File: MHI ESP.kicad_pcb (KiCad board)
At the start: 2 copper layers, 26 x 35 mm, 9 parts, among them J1 , U1 WeMos_D1_mini, U2 R-78E5.0-1.0, U3 DS18B20U, U4 TXB0104PW

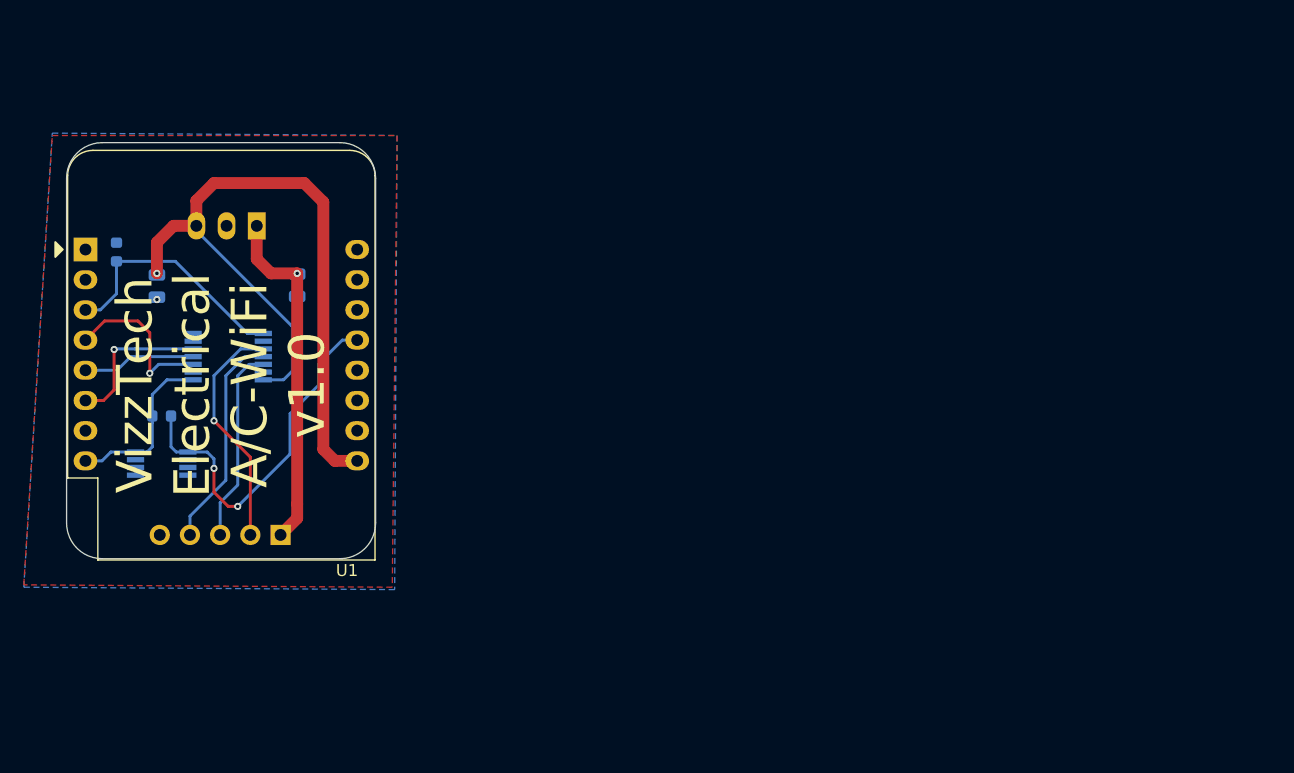
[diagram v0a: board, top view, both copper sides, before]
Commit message: Re-annotate schematic and update components on PCB, ready for new track layout
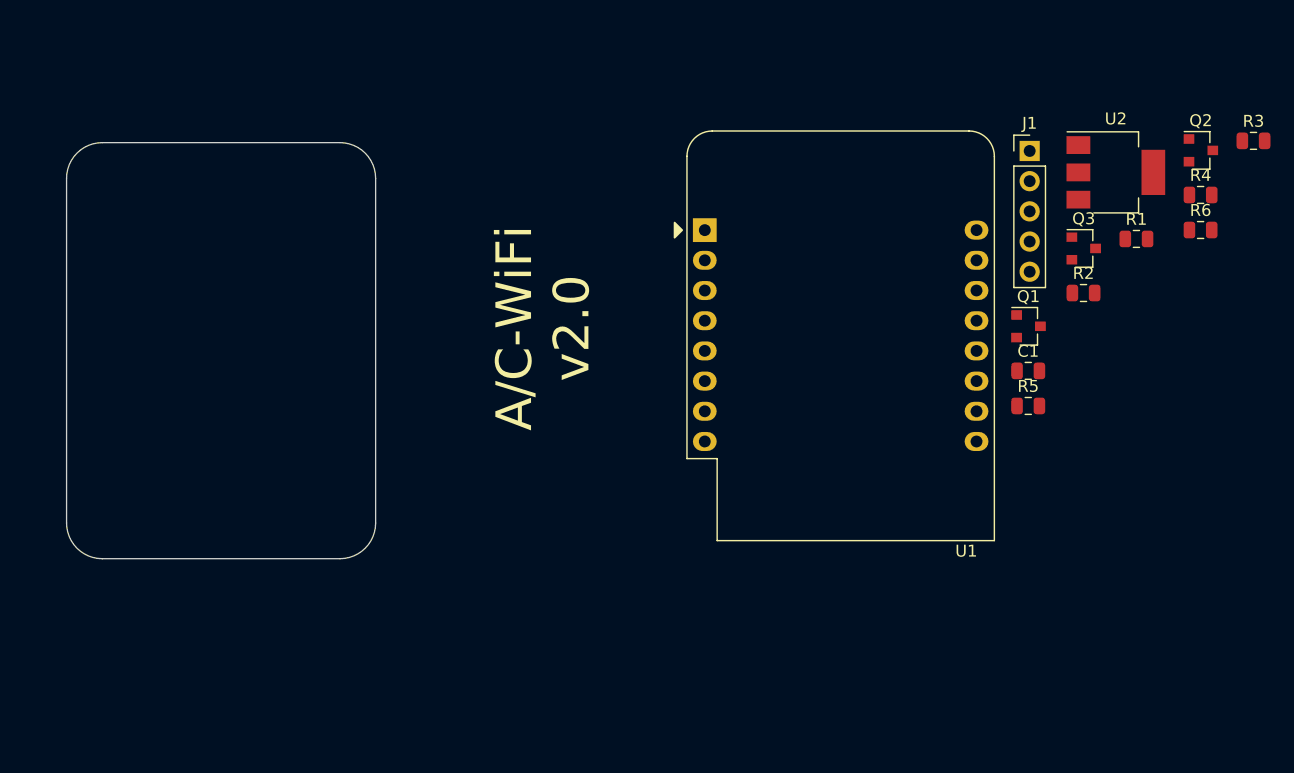
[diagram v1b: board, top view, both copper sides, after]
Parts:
- removed C2: 10uF, 0805, Capacitor_SMD:C_0805_2012Metric
- removed U3: DS18B20U, Package_SO:MSOP-8_3x3mm_P0.65mm
- removed U4: TXB0104PW, Package_SO:TSSOP-14_4.4x5mm_P0.65mm
- added Q1: BSS138, Package_TO_SOT_SMD:SOT-23, F.Cu at (192.9, 99.5)
- added Q2: BSS138, Package_TO_SOT_SMD:SOT-23, F.Cu at (207.4, 84.7)
- added Q3: BSS138, Package_TO_SOT_SMD:SOT-23, F.Cu at (197.6, 92.9)
- added R3: 10k, Resistor_SMD:R_0805_2012Metric, F.Cu at (211.8, 83.8)
- added R4: 10k, Resistor_SMD:R_0805_2012Metric, F.Cu at (207.4, 88.4)
- added R5: 10k, Resistor_SMD:R_0805_2012Metric, F.Cu at (192.9, 106.2)
- added R6: 10k, Resistor_SMD:R_0805_2012Metric, F.Cu at (207.4, 91.3)
- C1, J1: moved to F.Cu
- R1: value 100k, 0603 -> 10k; footprint Resistor_SMD:R_0603_1608Metric -> Resistor_SMD:R_0805_2012Metric; moved to F.Cu
- R2: value 4k7, 0603 -> 10k; footprint Resistor_SMD:R_0603_1608Metric -> Resistor_SMD:R_0805_2012Metric; moved to F.Cu
- U2: value R-78E5.0-1.0 -> LD1117S50TR; footprint Converter_DCDC:Converter_DCDC_RECOM_R-78E-0.5_THT -> Package_TO_SOT_SMD:SOT-223-3_TabPin2; moved to F.Cu
- moved R1 85.8 mm to (202.0, 92.1), turned to 0 degrees
- moved R2 78.2 mm to (197.6, 96.7)
- moved U2 72.4 mm to (200.3, 86.5), turned to 0 degrees
- moved J1 70.8 mm to (193.0, 84.7), turned to 0 degrees
- moved C1 61.9 mm to (192.9, 103.2), turned to 0 degrees
- moved U1 52.1 mm to (165.7, 91.4)
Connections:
- C1 pad 1: +12V -> +5V
- J1 pad 2: Net-(J1-Pad2) -> MHI-MOSI
- J1 pad 3: Net-(J1-Pad3) -> MHI-SCK
- J1 pad 4: Net-(J1-Pad4) -> MHI-MISO
- R1 pad 1: Net-(R1-Pad1) -> +3V3
- R1 pad 2: GND -> ESP-SCK
- R2 pad 2: Net-(R2-Pad2) -> ESP-MISO
- U1 pad 1: Net-(U1-Pad1) -> (no net)
- U1 pad 11: Net-(U1-Pad11) -> (no net)
- U1 pad 12: Net-(U1-Pad12) -> (no net)
- U1 pad 13: Net-(R2-Pad2) -> (no net)
- U1 pad 14: Net-(U1-Pad14) -> (no net)
- U1 pad 15: Net-(U1-Pad15) -> (no net)
- U1 pad 16: Net-(U1-Pad16) -> (no net)
- U1 pad 2: Net-(U1-Pad2) -> (no net)
- U1 pad 3: Net-(R1-Pad1) -> (no net)
- U1 pad 4: Net-(U1-Pad4) -> ESP-SCK
- U1 pad 5: Net-(U1-Pad5) -> ESP-MISO
- U1 pad 6: Net-(U1-Pad6) -> ESP-MOSI
- U1 pad 7: Net-(U1-Pad7) -> (no net)
- U2 pad 1: +12V -> GND
- U2 pad 2: GND -> +5V
- U2 pad 3: +5V -> +12V
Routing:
- net +5V: track 63.0 -> 0.00 mm, vias 1 -> 0
- net Net-(R2-Pad2): track 30.8 -> 0.00 mm, vias 2 -> 0
- net +12V: track 29.3 -> 0.00 mm, vias 1 -> 0
- net Net-(R1-Pad1): track 20.8 -> 0.00 mm
- net Net-(J1-Pad2): track 19.7 -> 0.00 mm, vias 1 -> 0
- net Net-(J1-Pad4): track 18.5 -> 0.00 mm
- net Net-(J1-Pad3): track 16.6 -> 0.00 mm
- net +3V3: track 14.5 -> 0.00 mm
- net Net-(U1-Pad4): track 13.9 -> 0.00 mm, vias 1 -> 0
- net Net-(U1-Pad6): track 12.8 -> 0.00 mm, vias 1 -> 0
- net Net-(U1-Pad5): track 9.54 -> 0.00 mm
- net GND: vias 1 -> 0
- removed copper zone on B.Cu, net GND
- removed copper zone on F.Cu, net GND
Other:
- board text added: "A/C-WiFi v2.0"
- board text removed: "VizzTech Electrical A/C-WiFi v1.0"

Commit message: Ready to route PCB v2.0
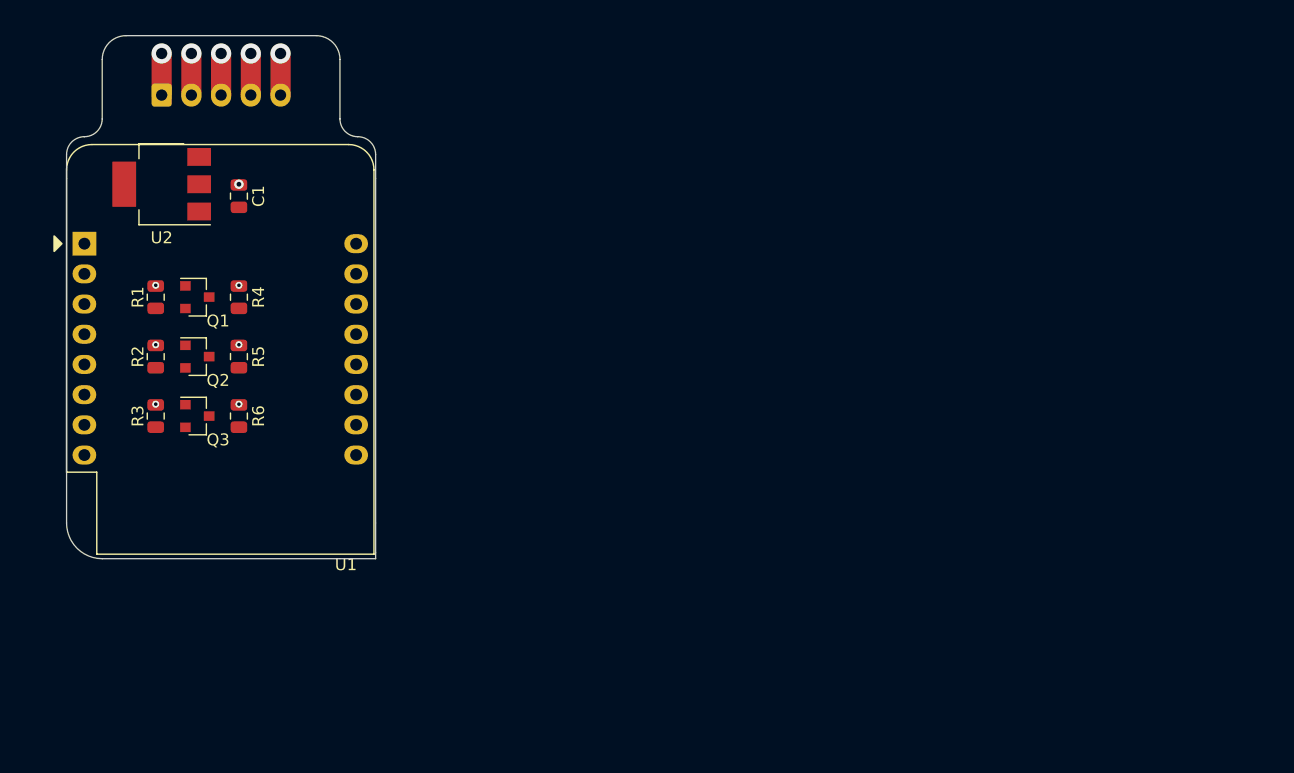
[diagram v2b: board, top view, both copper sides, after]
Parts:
- added REF**: OSHW-Logo_19x20mm_SilkScreen, Symbol:OSHW-Logo_19x20mm_SilkScreen, B.Cu at (125.0, 96.0)
- J1: footprint Connector_PinHeader_2.54mm:PinHeader_1x05_P2.54mm_Vertical -> Connector_JST:JST_XH_B5B-XH-A_1x05_P2.50mm_Vertical; moved to B.Cu
- moved R3 95.2 mm to (119.5, 107.0), turned to 270 degrees
- moved Q2 86.2 mm to (123.0, 102.0)
- moved R1 82.6 mm to (119.5, 97.0), turned to 270 degrees
- moved R6 82.4 mm to (126.5, 107.0), turned to 270 degrees
- moved R4 81.4 mm to (126.5, 97.0), turned to 270 degrees
- moved U2 80.3 mm to (120.0, 87.5), turned to 180 degrees
- moved R2 78.2 mm to (119.5, 102.0), turned to 270 degrees
- moved Q3 75.9 mm to (123.0, 107.0)
- moved J1 73.2 mm to (120.0, 80.0)
- moved Q1 70.0 mm to (123.0, 97.0)
- moved C1 68.0 mm to (126.5, 88.5), turned to 270 degrees
- moved R5 66.5 mm to (126.5, 102.0), turned to 270 degrees
- moved U1 52.2 mm to (113.5, 92.5)
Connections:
- J1 pad 2: MHI-MOSI -> MHI-SCK
- J1 pad 3: MHI-SCK -> MHI-MOSI
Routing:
- net MHI-SCK: track 0.00 -> 3.50 mm, vias 0 -> 1
- net MHI-MOSI: track 0.00 -> 3.50 mm, vias 0 -> 1
- net MHI-MISO: track 0.00 -> 3.50 mm, vias 0 -> 1
- net GND: track 0.00 -> 3.50 mm, vias 0 -> 1
- net +12V: track 0.00 -> 3.50 mm, vias 0 -> 2
- net +5V: vias 0 -> 4
- net +3V3: vias 0 -> 3
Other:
- board size 26 x 35 mm -> 26 x 44 mm

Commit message: PCB v2.0 - routing completed
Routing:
- net +5V: track 0.00 -> 41.2 mm
- net MHI-MOSI: track 3.50 -> 40.8 mm
- net MHI-MISO: track 3.50 -> 37.3 mm, vias 1 -> 3
- net +3V3: track 0.00 -> 26.8 mm
- net MHI-SCK: track 3.50 -> 29.3 mm
- net ESP-MOSI: track 0.00 -> 9.64 mm
- net ESP-SCK: track 0.00 -> 9.41 mm
- net ESP-MISO: track 0.00 -> 8.62 mm
- net +12V: track 3.50 -> 11.4 mm
- net GND: vias 1 -> 2
- added copper zone on B.Cu, net GND
- added copper zone on F.Cu, net GND
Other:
- net class Default: trace_width 0.25 -> 0.5
- rule trace_min: 0.2 -> 0.5
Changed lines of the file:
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@@
     (thickness 1.6)
     (drawings 24)
-    (tracks 18)
+    (tracks 78)
     (zones 0)
     (modules 14)
@@
   )
   (setup
-    (last_trace_width 0.25)
+    (last_trace_width 0.5)
     (trace_clearance 0.2)
     (zone_clearance 0.508)
     (zone_45_only no)
-    (trace_min 0.2)
+    (trace_min 0.5)
     (via_size 0.8)
     (via_drill 0.4)
@@
   (net_class Default "This is the default net class."
     (clearance 0.2)
-    (trace_width 0.25)
+    (trace_width 0.5)
     (via_dia 0.8)
     (via_drill 0.4)
     (uvia_dia 0.3)
     (uvia_drill 0.1)
+    (diff_pair_width 0.5)
+    (diff_pair_gap 0.25)
     (add_net +12V)
     (add_net +3V3)
@@
     (add_net MHI-MOSI)
     (add_net MHI-SCK)
-    (add_net "Net-(U1-Pad1)")
-    (add_net "Net-(U1-Pad11)")
-    (add_net "Net-(U1-Pad12)")
-    (add_net "Net-(U1-Pad13)")
-    (add_net "Net-(U1-Pad14)")
-    (add_net "Net-(U1-Pad15)")
-    (add_net "Net-(U1-Pad16)")
-    (add_net "Net-(U1-Pad2)")
-    (add_net "Net-(U1-Pad3)")
-    (add_net "Net-(U1-Pad7)")
   )
   (module Symbol:OSHW-Logo_19x20mm_SilkScreen (layer B.Cu)
@@
   (gr_line (start 135 119) (end 115 119) (layer Edge.Cuts) (width 0.05))
   (gr_line (start 138 87) (end 138 116) (layer Edge.Cuts) (width 0.05))
+  (via (at 129 103) (size 0.6) (drill 0.3) (layers F.Cu B.Cu) (net 3))
+  (via (at 133 101.5) (size 0.6) (drill 0.3) (layers F.Cu B.Cu) (net 3))
+  (segment (start 124.9375 107.9375) (end 126.5 107.9375) (width 0.5) (layer F.Cu) (net 5))
+  (segment (start 124 107) (end 124.9375 107.9375) (width 0.5) (layer F.Cu) (net 5))
+  (segment (start 124.9375 102.9375) (end 126.5 102.9375) (width 0.5) (layer F.Cu) (net 3))
+  (segment (start 124 102) (end 124.9375 102.9375) (width 0.5) (layer F.Cu) (net 3))
   (segment (start 130 76.5) (end 130 80) (width 1.7) (layer F.Cu) (net 1))
-  (segment (start 127.5 76.5) (end 127.5 80) (width 1.7) (layer F.Cu) (net 3))
-  (segment (start 125 76.5) (end 125 80) (width 1.7) (layer F.Cu) (net 5))
-  (segment (start 122.5 76.5) (end 122.5 80) (width 1.7) (layer F.Cu) (net 4))
-  (via (at 120 76.5) (size 1.7) (drill 0.95) (layers F.Cu B.Cu) (net 6))
-  (via (at 122.5 76.5) (size 1.7) (drill 0.95) (layers F.Cu B.Cu) (net 4))
-  (via (at 125 76.5) (size 1.7) (drill 0.95) (layers F.Cu B.Cu) (net 5))
-  (via (at 127.5 76.5) (size 1.7) (drill 0.95) (layers F.Cu B.Cu) (net 3))
   (via (at 130 76.5) (size 1.7) (drill 0.95) (layers F.Cu B.Cu) (net 1))
-  (via (at 120 80) (size 0.8) (drill 0.4) (layers F.Cu B.Cu) (net 6))
+  (via (at 117 78) (size 1) (drill 0.5) (layers F.Cu B.Cu) (net 1))
   (via (at 126.5 106) (size 0.6) (drill 0.3) (layers F.Cu B.Cu) (net 2))
   (via (at 126.5 101) (size 0.6) (drill 0.3) (layers F.Cu B.Cu) (net 2))
   (via (at 126.5 96) (size 0.6) (drill 0.3) (layers F.Cu B.Cu) (net 2))
   (via (at 126.5 87.5) (size 0.8) (drill 0.4) (layers F.Cu B.Cu) (net 2))
+  (segment (start 116.85 87.5) (end 126.5 87.5) (width 0.75) (layer F.Cu) (net 2))
+  (segment (start 126.5 87.5) (end 126.5 106) (width 0.75) (layer B.Cu) (net 2))
+  (segment (start 126.5 106) (end 126.5 108.5) (width 0.75) (layer B.Cu) (net 2))
+  (segment (start 128.28 110.28) (end 136.36 110.28) (width 0.75) (layer B.Cu) (net 2))
+  (segment (start 126.5 108.5) (end 128.28 110.28) (width 0.75) (layer B.Cu) (net 2))
+  (segment (start 127.5 76.5) (end 127.5 80) (width 1.7) (layer F.Cu) (net 3))
+  (via (at 127.5 76.5) (size 1.7) (drill 0.95) (layers F.Cu B.Cu) (net 3))
+  (segment (start 128.9375 102.9375) (end 129 103) (width 0.5) (layer F.Cu) (net 3))
+  (segment (start 126.5 102.9375) (end 128.9375 102.9375) (width 0.5) (layer F.Cu) (net 3))
+  (segment (start 131.5 103) (end 133 101.5) (width 0.5) (layer B.Cu) (net 3))
+  (segment (start 129 103) (end 131.5 103) (width 0.5) (layer B.Cu) (net 3))
+  (segment (start 133 86.975) (end 133 101.5) (width 0.5) (layer F.Cu) (net 3))
+  (segment (start 127.5 80) (end 127.5 81.475) (width 0.5) (layer F.Cu) (net 3))
+  (segment (start 127.5 81.475) (end 133 86.975) (width 0.5) (layer F.Cu) (net 3))
+  (segment (start 122.5 76.5) (end 122.5 80) (width 1.7) (layer F.Cu) (net 4))
+  (via (at 122.5 76.5) (size 1.7) (drill 0.95) (layers F.Cu B.Cu) (net 4))
+  (segment (start 124.9375 97.9375) (end 126.5 97.9375) (width 0.5) (layer F.Cu) (net 4))
+  (segment (start 124 97) (end 124.9375 97.9375) (width 0.5) (layer F.Cu) (net 4))
+  (segment (start 128.5625 97.9375) (end 126.5 97.9375) (width 0.5) (layer F.Cu) (net 4))
+  (segment (start 122.5 81.475) (end 127.5 86.475) (width 0.5) (layer F.Cu) (net 4))
+  (segment (start 122.5 80) (end 122.5 81.475) (width 0.5) (layer F.Cu) (net 4))
+  (segment (start 127.5 86.475) (end 127.5 86.5) (width 0.5) (layer F.Cu) (net 4))
+  (segment (start 127.5 86.5) (end 129 88) (width 0.5) (layer F.Cu) (net 4))
+  (segment (start 129 88) (end 129 97.5) (width 0.5) (layer F.Cu) (net 4))
+  (segment (start 129 97.5) (end 128.5625 97.9375) (width 0.5) (layer F.Cu) (net 4))
+  (segment (start 125 76.5) (end 125 80) (width 1.7) (layer F.Cu) (net 5))
+  (via (at 125 76.5) (size 1.7) (drill 0.95) (layers F.Cu B.Cu) (net 5))
+  (segment (start 130.0625 107.9375) (end 126.5 107.9375) (width 0.5) (layer F.Cu) (net 5))
+  (segment (start 131 107) (end 130.0625 107.9375) (width 0.5) (layer F.Cu) (net 5))
+  (segment (start 131 87.475) (end 131 107) (width 0.5) (layer F.Cu) (net 5))
+  (segment (start 125 80) (end 125 81.475) (width 0.5) (layer F.Cu) (net 5))
+  (segment (start 125 81.475) (end 131 87.475) (width 0.5) (layer F.Cu) (net 5))
+  (via (at 120 76.5) (size 1.7) (drill 0.95) (layers F.Cu B.Cu) (net 6))
+  (via (at 120 80) (size 0.8) (drill 0.4) (layers F.Cu B.Cu) (net 6))
   (segment (start 120 76.5) (end 120 80) (width 1.7) (layer F.Cu) (net 6))
+  (segment (start 120.7 85.2) (end 123.15 85.2) (width 1) (layer F.Cu) (net 6))
+  (segment (start 120 80) (end 120 84.5) (width 1) (layer F.Cu) (net 6))
+  (segment (start 120 84.5) (end 120.7 85.2) (width 1) (layer F.Cu) (net 6))
+  (segment (start 117.5625 97.9375) (end 119.5 97.9375) (width 0.5) (layer F.Cu) (net 7))
+  (segment (start 113.5 100.12) (end 115.38 100.12) (width 0.5) (layer F.Cu) (net 7))
+  (segment (start 115.38 100.12) (end 117.5625 97.9375) (width 0.5) (layer F.Cu) (net 7))
+  (segment (start 119.5125 97.95) (end 119.5 97.9375) (width 0.5) (layer F.Cu) (net 7))
+  (segment (start 122 97.95) (end 119.5125 97.95) (width 0.5) (layer F.Cu) (net 7))
   (via (at 119.5 106) (size 0.6) (drill 0.3) (layers F.Cu B.Cu) (net 8))
   (via (at 119.5 101) (size 0.6) (drill 0.3) (layers F.Cu B.Cu) (net 8))
   (via (at 119.5 96) (size 0.6) (drill 0.3) (layers F.Cu B.Cu) (net 8))
+  (segment (start 119.5 96) (end 119.5 106) (width 0.75) (layer B.Cu) (net 8))
+  (segment (start 117.72 110.28) (end 113.5 110.28) (width 0.75) (layer B.Cu) (net 8))
+  (segment (start 119.5 106) (end 119.5 108.5) (width 0.75) (layer B.Cu) (net 8))
+  (segment (start 119.5 108.5) (end 117.72 110.28) (width 0.75) (layer B.Cu) (net 8))
+  (segment (start 119.55 101.05) (end 119.5 101) (width 0.5) (layer F.Cu) (net 8))
+  (segment (start 122 101.05) (end 119.55 101.05) (width 0.5) (layer F.Cu) (net 8))
+  (segment (start 119.5125 96.05) (end 119.5 96.0625) (width 0.5) (layer F.Cu) (net 8))
+  (segment (start 122 96.05) (end 119.5125 96.05) (width 0.5) (layer F.Cu) (net 8))
+  (segment (start 119.55 106.05) (end 119.5 106) (width 0.5) (layer F.Cu) (net 8))
+  (segment (start 122 106.05) (end 119.55 106.05) (width 0.5) (layer F.Cu) (net 8))
+  (segment (start 113.7775 102.9375) (end 113.5 102.66) (width 0.5) (layer F.Cu) (net 9))
+  (segment (start 119.5 102.9375) (end 113.7775 102.9375) (width 0.5) (layer F.Cu) (net 9))
+  (segment (start 119.5125 102.95) (end 119.5 102.9375) (width 0.5) (layer F.Cu) (net 9))
+  (segment (start 122 102.95) (end 119.5125 102.95) (width 0.5) (layer F.Cu) (net 9))
+  (segment (start 117.9375 107.9375) (end 119.5 107.9375) (width 0.5) (layer F.Cu) (net 10))
+  (segment (start 113.5 105.2) (end 115.2 105.2) (width 0.5) (layer F.Cu) (net 10))
+  (segment (start 115.2 105.2) (end 117.9375 107.9375) (width 0.5) (layer F.Cu) (net 10))
+  (segment (start 119.5125 107.95) (end 119.5 107.9375) (width 0.5) (layer F.Cu) (net 10))
+  (segment (start 122 107.95) (end 119.5125 107.95) (width 0.5) (layer F.Cu) (net 10))
+  (zone (net 1) (net_name GND) (layer B.Cu) (hatch edge 0.508)
+    (connect_pads (clearance 0.508))
+    (min_thickness 0.2)
+    (fill yes (arc_segments 32) (thermal_gap 0.508) (thermal_bridge_width 0.508))
+    (polygon
+      (pts
+        (xy 138 119) (xy 138 75) (xy 112 75) (xy 112 119)
+      )
+    )
+  )
+  (zone (net 1) (net_name GND) (layer F.Cu) (hatch edge 0.508)
+    (connect_pads (clearance 0.508))
+    (min_thickness 0.254)
+    (fill yes (arc_segments 32) (thermal_gap 0.508) (thermal_bridge_width 0.508))
+    (polygon
+      (pts
+        (xy 138 119) (xy 138 75) (xy 112 75) (xy 112 119)
+      )
+    )
+  )
 )
